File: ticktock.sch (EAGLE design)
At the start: 64 parts, among them IC1 ATMEGA644A, IC2 AD8611R, IC3 REF200U, J1 AVR_SPI_PRG_6NS, Q1 MOSFET-NCHANNEL2N7002PW, Q2 MOSFET-NCHANNELBSS138, Q3 MOSFET-NCHANNELBSS138, U1 MAX232SOIC16, U2 OSCILLATORSMD, U3 FT232RLSSOP, U4 BMP180

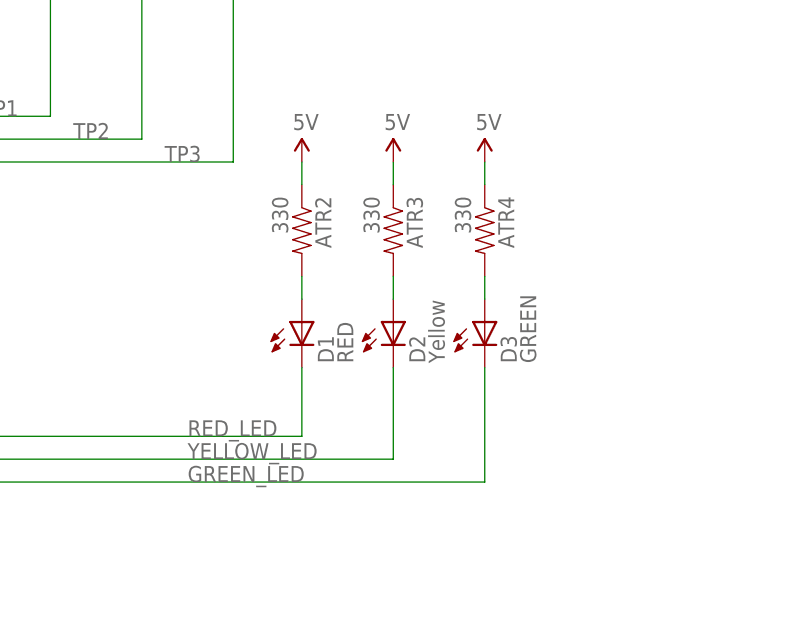
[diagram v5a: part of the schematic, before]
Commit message: swap LEDs and resistors to get LEDs into PCB corner
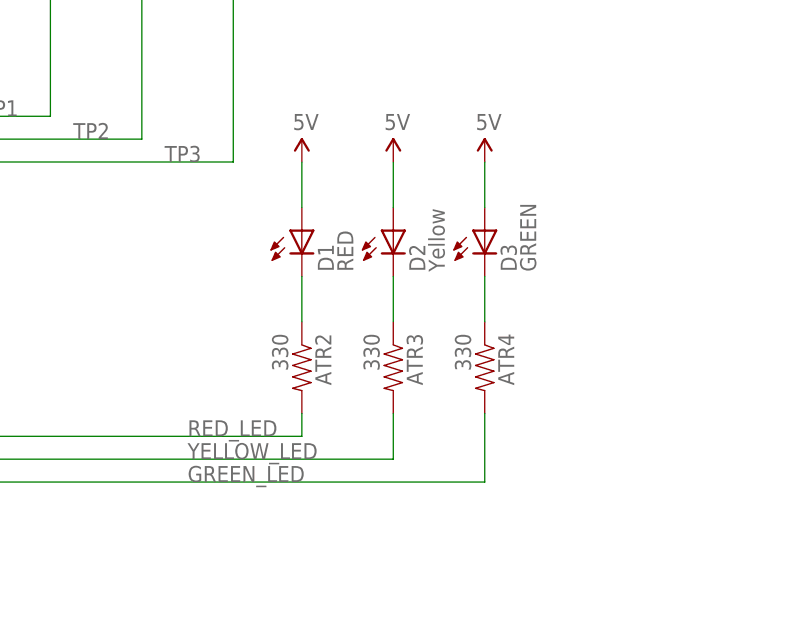
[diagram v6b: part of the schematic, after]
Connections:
- net 5V: now also D1.A, D2.A, D3.A; no longer ATR2.1, ATR3.1, ATR4.1
- net GREEN_LED: now also ATR4.2; no longer D3.C
- net N$16: now also ATR4.1, D3.C; no longer ATR2.2, D1.A
- net N$20: now also ATR3.1, D2.C; no longer ATR3.2, D2.A
- net N$21: now also ATR2.1, D1.C; no longer ATR4.2, D3.A
- net RED_LED: now also ATR2.2; no longer D1.C
- net YELLOW_LED: now also ATR3.2; no longer D2.C
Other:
- moved on the sheet: ATR2, ATR3, ATR4, D1, D2, D3
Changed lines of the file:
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@@
 <instance part="SUPPLY26" gate="G$1" x="429.26" y="180.34"/>
 <instance part="SUPPLY27" gate="G$1" x="487.68" y="180.34"/>
-<instance part="ATR2" gate="G$1" x="238.76" y="162.56" rot="R270"/>
-<instance part="ATR3" gate="G$1" x="248.92" y="162.56" rot="R270"/>
-<instance part="ATR4" gate="G$1" x="259.08" y="162.56" rot="R270"/>
-<instance part="D2" gate="G$1" x="248.92" y="152.4"/>
-<instance part="D1" gate="G$1" x="238.76" y="152.4"/>
-<instance part="D3" gate="G$1" x="259.08" y="152.4"/>
+<instance part="ATR2" gate="G$1" x="238.76" y="147.32" rot="R270"/>
+<instance part="ATR3" gate="G$1" x="248.92" y="147.32" rot="R270"/>
+<instance part="ATR4" gate="G$1" x="259.08" y="147.32" rot="R270"/>
+<instance part="D2" gate="G$1" x="248.92" y="162.56"/>
+<instance part="D1" gate="G$1" x="238.76" y="162.56"/>
+<instance part="D3" gate="G$1" x="259.08" y="162.56"/>
 <instance part="SUPPLY28" gate="G$1" x="238.76" y="170.18"/>
 <instance part="SUPPLY29" gate="G$1" x="248.92" y="170.18"/>
@@
 </segment>
 <segment>
-<pinref part="SUPPLY28" gate="G$1" pin="5V"/>
-<pinref part="ATR2" gate="G$1" pin="1"/>
-<wire x1="238.76" y1="170.18" x2="238.76" y2="167.64" width="0.1524" layer="91"/>
-</segment>
-<segment>
-<pinref part="SUPPLY29" gate="G$1" pin="5V"/>
-<pinref part="ATR3" gate="G$1" pin="1"/>
-<wire x1="248.92" y1="170.18" x2="248.92" y2="167.64" width="0.1524" layer="91"/>
-</segment>
-<segment>
-<pinref part="SUPPLY30" gate="G$1" pin="5V"/>
-<pinref part="ATR4" gate="G$1" pin="1"/>
-<wire x1="259.08" y1="170.18" x2="259.08" y2="167.64" width="0.1524" layer="91"/>
-</segment>
-<segment>
 <pinref part="JP8" gate="G$1" pin="7"/>
 <wire x1="408.94" y1="121.92" x2="421.64" y2="121.92" width="0.1524" layer="91"/>
@@
 <pinref part="SUPPLY15" gate="G$1" pin="5V"/>
 <wire x1="210.82" y1="73.66" x2="210.82" y2="91.44" width="0.1524" layer="91"/>
+</segment>
+<segment>
+<pinref part="SUPPLY28" gate="G$1" pin="5V"/>
+<pinref part="D1" gate="G$1" pin="A"/>
+<wire x1="238.76" y1="170.18" x2="238.76" y2="165.1" width="0.1524" layer="91"/>
+</segment>
+<segment>
+<pinref part="SUPPLY29" gate="G$1" pin="5V"/>
+<pinref part="D2" gate="G$1" pin="A"/>
+<wire x1="248.92" y1="170.18" x2="248.92" y2="165.1" width="0.1524" layer="91"/>
+</segment>
+<segment>
+<pinref part="SUPPLY30" gate="G$1" pin="5V"/>
+<pinref part="D3" gate="G$1" pin="A"/>
+<wire x1="259.08" y1="170.18" x2="259.08" y2="165.1" width="0.1524" layer="91"/>
 </segment>
 </net>
@@
 </segment>
 </net>
-<net name="N$16" class="0">
-<segment>
-<pinref part="ATR2" gate="G$1" pin="2"/>
-<pinref part="D1" gate="G$1" pin="A"/>
-<wire x1="238.76" y1="157.48" x2="238.76" y2="154.94" width="0.1524" layer="91"/>
-</segment>
-</net>
-<net name="N$20" class="0">
-<segment>
-<pinref part="ATR3" gate="G$1" pin="2"/>
-<pinref part="D2" gate="G$1" pin="A"/>
-<wire x1="248.92" y1="157.48" x2="248.92" y2="154.94" width="0.1524" layer="91"/>
-</segment>
-</net>
-<net name="N$21" class="0">
-<segment>
-<pinref part="ATR4" gate="G$1" pin="2"/>
-<pinref part="D3" gate="G$1" pin="A"/>
-<wire x1="259.08" y1="157.48" x2="259.08" y2="154.94" width="0.1524" layer="91"/>
-</segment>
-</net>
 <net name="YELLOW_LED" class="0">
 <segment>
-<pinref part="D2" gate="G$1" pin="C"/>
-<wire x1="248.92" y1="147.32" x2="248.92" y2="137.16" width="0.1524" layer="91"/>
 <pinref part="IC1" gate="G$1" pin="(PCINT21/TDI)PC5"/>
 <wire x1="248.92" y1="137.16" x2="165.1" y2="137.16" width="0.1524" layer="91"/>
 <label x="226.06" y="137.16" size="1.778" layer="95"/>
+<pinref part="ATR3" gate="G$1" pin="2"/>
+<wire x1="248.92" y1="142.24" x2="248.92" y2="137.16" width="0.1524" layer="91"/>
 </segment>
 </net>
 <net name="GREEN_LED" class="0">
 <segment>
-<pinref part="D3" gate="G$1" pin="C"/>
-<wire x1="259.08" y1="147.32" x2="259.08" y2="134.62" width="0.1524" layer="91"/>
 <pinref part="IC1" gate="G$1" pin="(PCINT20/TDO)PC4"/>
 <wire x1="165.1" y1="134.62" x2="259.08" y2="134.62" width="0.1524" layer="91"/>
 <label x="226.06" y="134.62" size="1.778" layer="95"/>
+<pinref part="ATR4" gate="G$1" pin="2"/>
+<wire x1="259.08" y1="142.24" x2="259.08" y2="134.62" width="0.1524" layer="91"/>
 </segment>
 </net>
@@
 <wire x1="165.1" y1="139.7" x2="238.76" y2="139.7" width="0.1524" layer="91"/>
 <label x="226.06" y="139.7" size="1.778" layer="95"/>
-<pinref part="D1" gate="G$1" pin="C"/>
-<wire x1="238.76" y1="147.32" x2="238.76" y2="139.7" width="0.1524" layer="91"/>
+<pinref part="ATR2" gate="G$1" pin="2"/>
+<wire x1="238.76" y1="142.24" x2="238.76" y2="139.7" width="0.1524" layer="91"/>
 </segment>
 </net>
@@
 </segment>
 </net>
+<net name="N$16" class="0">
+<segment>
+<pinref part="D3" gate="G$1" pin="C"/>
+<pinref part="ATR4" gate="G$1" pin="1"/>
+<wire x1="259.08" y1="157.48" x2="259.08" y2="152.4" width="0.1524" layer="91"/>
+</segment>
+</net>
+<net name="N$20" class="0">
+<segment>
+<pinref part="D2" gate="G$1" pin="C"/>
+<pinref part="ATR3" gate="G$1" pin="1"/>
+<wire x1="248.92" y1="157.48" x2="248.92" y2="152.4" width="0.1524" layer="91"/>
+</segment>
+</net>
+<net name="N$21" class="0">
+<segment>
+<pinref part="D1" gate="G$1" pin="C"/>
+<pinref part="ATR2" gate="G$1" pin="1"/>
+<wire x1="238.76" y1="157.48" x2="238.76" y2="152.4" width="0.1524" layer="91"/>
+</segment>
+</net>

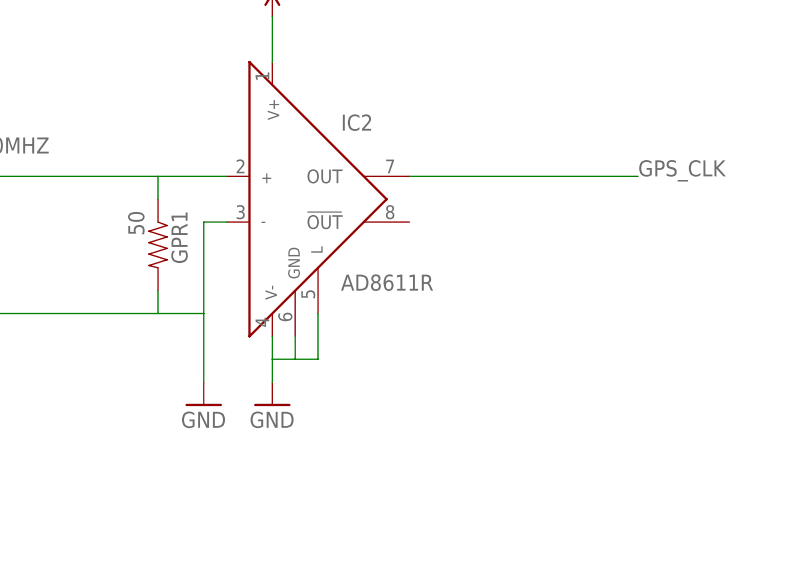
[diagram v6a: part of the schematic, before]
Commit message: Replace SO8 package of ultrafast comparator with MSOP8 package.
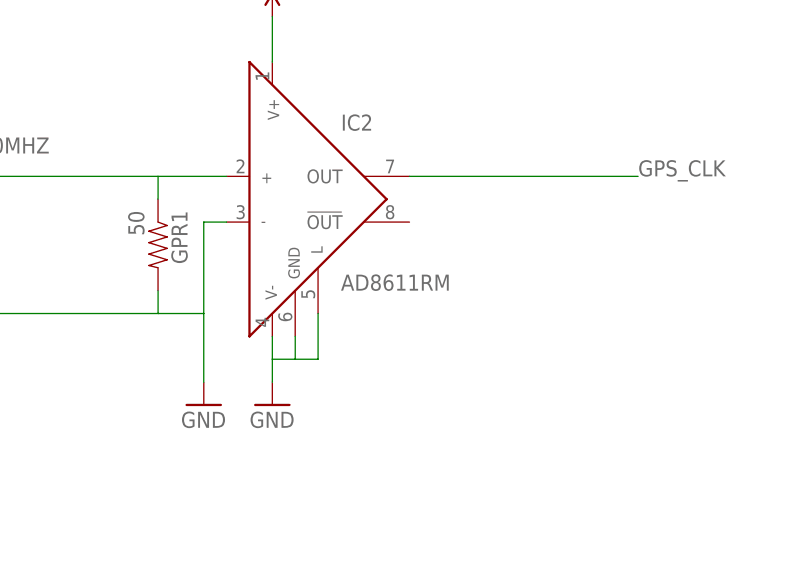
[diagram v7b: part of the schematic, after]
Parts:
- IC2: value AD8611R -> AD8611RM; device analog-devices:AD8611R -> analog-devices:AD8611RM
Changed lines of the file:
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@@
 <?xml version="1.0" encoding="utf-8"?>
 <!DOCTYPE eagle SYSTEM "eagle.dtd">
-<eagle version="6.5.0">
+<eagle version="6.4">
 <drawing>
 <settings>
@@
 <part name="ATC4" library="SparkFun-Capacitors" deviceset="CAP" device="0805" value="0.01uF"/>
 <part name="JP2" library="SparkFun-Connectors" deviceset="M03" device="LOCK"/>
-<part name="IC2" library="analog-devices" deviceset="AD8611" device="R"/>
+<part name="IC2" library="analog-devices" deviceset="AD8611" device="RM" value="AD8611RM"/>
 <part name="GPR1" library="SparkFun-Resistors" deviceset="RESISTOR" device="0805-RES" value="50"/>
 <part name="GND17" library="SparkFun-Aesthetics" deviceset="GND" device=""/>

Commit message: Add power to pin 4 of FTDI chip.
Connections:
- net 5V: now also U3.VCCIO
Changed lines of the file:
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@@
-</segment>
-<segment>
-<wire x1="50.8" y1="48.26" x2="58.42" y2="48.26" width="0.1524" layer="91"/>
-<pinref part="SUPPLY7" gate="G$1" pin="5V"/>
 </segment>
 <segment>
@@
 <wire x1="259.08" y1="170.18" x2="259.08" y2="165.1" width="0.1524" layer="91"/>
 </segment>
+<segment>
+<pinref part="U3" gate="G$1" pin="VCCIO"/>
+<pinref part="SUPPLY7" gate="G$1" pin="5V"/>
+<wire x1="58.42" y1="48.26" x2="50.8" y2="48.26" width="0.1524" layer="91"/>
+</segment>
 </net>
